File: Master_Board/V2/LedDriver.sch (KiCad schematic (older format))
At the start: 12 parts, among them J1101 649002227222, U1101 AL8807W5-7

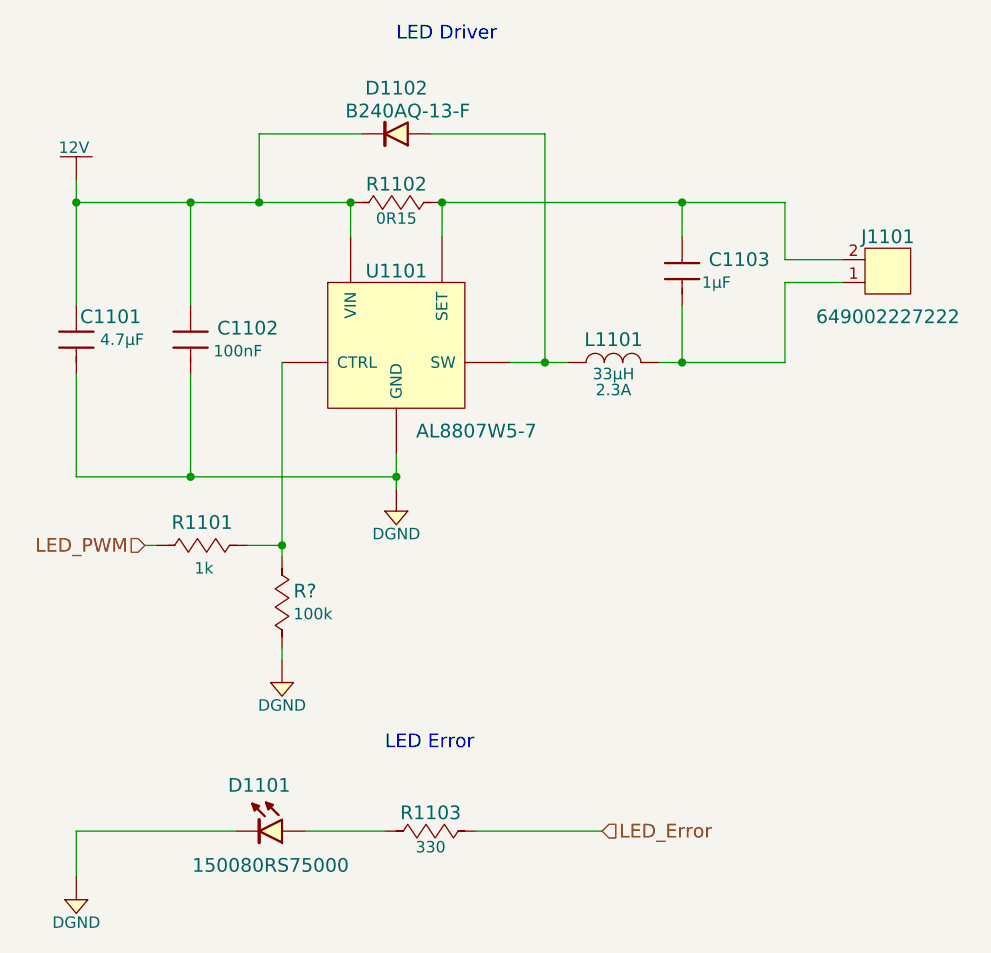
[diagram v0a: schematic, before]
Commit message: Place part in PCB
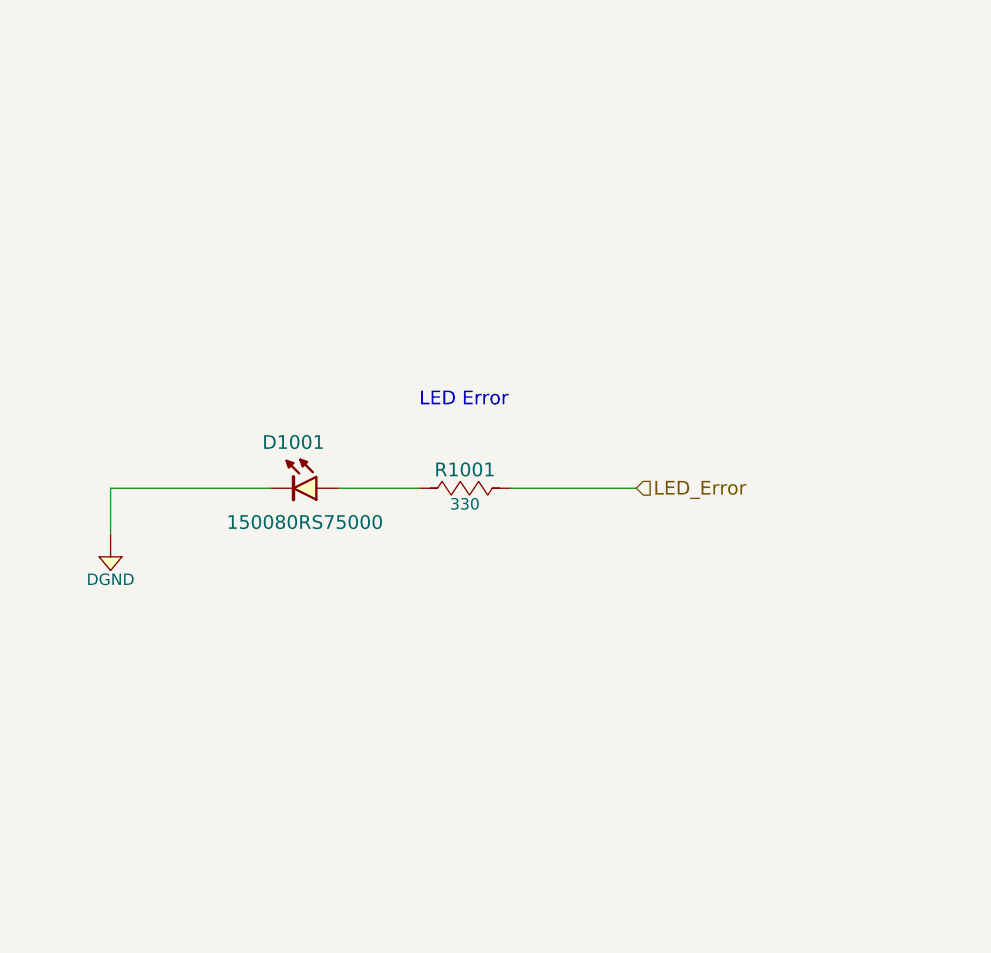
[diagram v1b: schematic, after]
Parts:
- removed C1101: 885012107018, Capacitors:C0805, symbol 885012107018
- removed C1102: 885012207098, Capacitors:C0805, symbol 885012207098
- removed C1103: 885012107015, Capacitors:C0805, symbol 885012107015
- removed D1102: B240AQ-13-F, Diodes:DO-214AC_SMA, symbol B240AQ-13-F
- removed J1101: 649002227222, Connectors:649002227222, symbol 649002227222
- removed L1101: 7447715330, Inductors:IND_1245, symbol 7447715330
- removed R1101: RC0805JR-071KL, Resistors:R0805, symbol RC0805JR-071KL
- removed R1102: RL0805FR-070R15L, Resistors:R0805, symbol RL0805FR-070R15L
- removed R?: RC0805JR-07100KL, Resistors:R0805, symbol RC0805JR-07100KL
- removed U1101: AL8807W5-7, IC:SOT-23-5, symbol AL8807W5-7
- renumbered D1101 to D1001, R1103 to R1001
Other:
- note removed: "LED Driver"
- moved on the sheet: D1001, R1001

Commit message: Done placing parts on PCB
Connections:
- net DGND: now also R1001.1; no longer D1001.1 (Cathode)
- net LED_Error: now also D1001.2 (Anode); no longer R1001.2
- new net: D1001.1 (Cathode), R1001.2
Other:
- moved on the sheet: D1001, R1001
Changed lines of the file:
@@
 L 150080RS75000 D1001
 U 1 1 594D45D6
-P 5350 3700
-F 0 "D1001" H 5350 3500 60  0000 C CNN
-F 1 "150080RS75000" H 5300 3850 60  0000 C CNN
-F 2 "Diodes:LED_0805_RED" H 5360 2620 60  0001 C CNN
-F 3 "http://katalog.we-online.de/led/datasheet/150080RS75000.pdf" H 5360 2520 60  0001 C CNN
-F 4 "Digikey" H 5360 3120 60  0001 C CNN "Supplier"
-F 5 "732-4984-1-ND" H 5360 3020 60  0001 C CNN "Supplier Part Number"
-F 6 "Wurth Electronics Inc." H 5360 2920 60  0001 C CNN "Manufacturer"
-F 7 "150080RS75000" H 5360 2820 60  0001 C CNN "Manufacturer Part Number"
-F 8 "LED RED CLEAR 0805 SMD" H 5360 2720 60  0001 C CNN "Description"
-F 9 "RED" H 5350 3400 60  0001 C CNN "Color"
-F 10 "2V" H 5350 3300 60  0001 C CNN "Voltage - Forward (Vf) (Typ)"
-	1    5350 3700
+P 6100 3700
+F 0 "D1001" H 6100 3500 60  0000 C CNN
+F 1 "150080RS75000" H 6050 3850 60  0001 C CNN
+F 2 "Diodes:LED_0805_RED" H 6110 2620 60  0001 C CNN
+F 3 "http://katalog.we-online.de/led/datasheet/150080RS75000.pdf" H 6110 2520 60  0001 C CNN
+F 4 "Digikey" H 6110 3120 60  0001 C CNN "Supplier"
+F 5 "732-4984-1-ND" H 6110 3020 60  0001 C CNN "Supplier Part Number"
+F 6 "Wurth Electronics Inc." H 6110 2920 60  0001 C CNN "Manufacturer"
+F 7 "150080RS75000" H 6110 2820 60  0001 C CNN "Manufacturer Part Number"
+F 8 "LED RED CLEAR 0805 SMD" H 6110 2720 60  0001 C CNN "Description"
+F 9 "RED" H 6100 3400 60  0000 C CNN "Color"
+F 10 "2V" H 6100 3300 60  0001 C CNN "Voltage - Forward (Vf) (Typ)"
+	1    6100 3700
 	-1   0    0    1
 $EndComp
@@
 L RC0805JR-07330RL R1001
 U 1 1 594D472A
-P 6100 3700
-F 0 "R1001" H 6100 3780 60  0000 C CNN
-F 1 "RC0805JR-07330RL" H 6100 3400 50  0001 C CNN
-F 2 "Resistors:R0805" H 6100 2800 30  0001 C CNN
-F 3 "http://www.yageo.com/documents/recent/PYu-RC_Group_51_RoHS_L_7.pdf" H 6100 2750 30  0001 C CNN
-F 4 "Digikey" H 6100 3300 60  0001 C CNN "Supplier"
-F 5 "311-330ARCT-ND" H 6100 3200 60  0001 C CNN "Supplier Part Number"
-F 6 "Yageo" H 6100 3100 60  0001 C CNN "Manufacturer"
-F 7 "RC0805JR-07330RL" H 6100 3000 60  0001 C CNN "Manufacturer Part Number"
-F 8 "RES SMD 330 OHM 5% 1/8W 0805" H 6100 2900 60  0001 C CNN "Description"
-F 9 "330" H 6100 3630 50  0000 C CNN "Resistance (Ohms)"
-F 10 "±5%" H 6510 3620 50  0001 C CNN "Tolerance (%)"
-F 11 "1/8W" H 6100 3560 50  0001 C CNN "Puissance (Watts)"
-	1    6100 3700
+P 5450 3700
+F 0 "R1001" H 5450 3780 60  0000 C CNN
+F 1 "RC0805JR-07330RL" H 5450 3400 50  0001 C CNN
+F 2 "Resistors:R0805" H 5450 2800 30  0001 C CNN
+F 3 "http://www.yageo.com/documents/recent/PYu-RC_Group_51_RoHS_L_7.pdf" H 5450 2750 30  0001 C CNN
+F 4 "Digikey" H 5450 3300 60  0001 C CNN "Supplier"
+F 5 "311-330ARCT-ND" H 5450 3200 60  0001 C CNN "Supplier Part Number"
+F 6 "Yageo" H 5450 3100 60  0001 C CNN "Manufacturer"
+F 7 "RC0805JR-07330RL" H 5450 3000 60  0001 C CNN "Manufacturer Part Number"
+F 8 "RES SMD 330 OHM 5% 1/8W 0805" H 5450 2900 60  0001 C CNN "Description"
+F 9 "330" H 5450 3630 50  0000 C CNN "Resistance (Ohms)"
+F 10 "±5%" H 5860 3620 50  0001 C CNN "Tolerance (%)"
+F 11 "1/8W" H 5450 3560 50  0001 C CNN "Puissance (Watts)"
+	1    5450 3700
 	1    0    0    -1
 $EndComp
 Wire Wire Line
-	5900 3700 5550 3700
+	5650 3700 6000 3700
 Text HLabel 6850 3700 2    60   Input ~ 0
 LED_Error
